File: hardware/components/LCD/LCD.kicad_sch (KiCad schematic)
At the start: 8 parts, among them SW1 slide, SW3 push

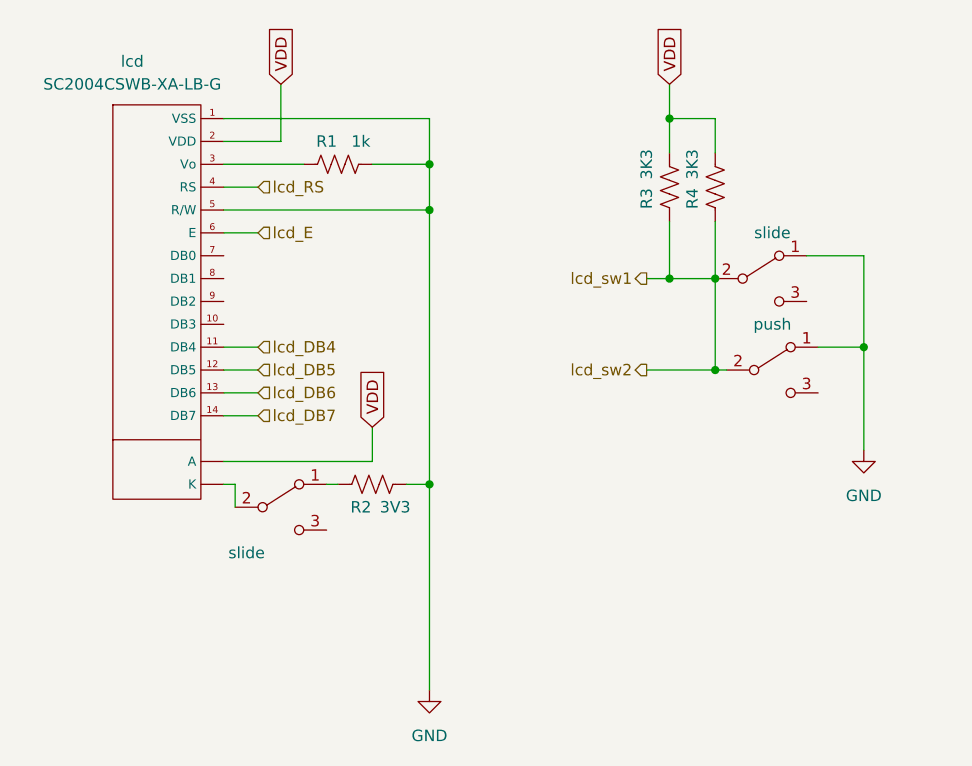
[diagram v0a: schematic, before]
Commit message: RP2040・LiPo・LoRa・ModuleIF・LCDのLCSC割り当て完了しました．基板設計中に確認していただきたいです． 何点か変更があります．LiPoPowerSimpleの充放電ICのProg周辺の抵抗値がLiPoPowerと異なっていたので合わせてしまっています． 今，ModuleIFのロードセルが指定されていたものではJLCPCBに在庫がなく，同じシリーズの在庫が多少残っているものを登録してます．そのためフットプリントと整合してません．別の物使うか判断をお願いします．
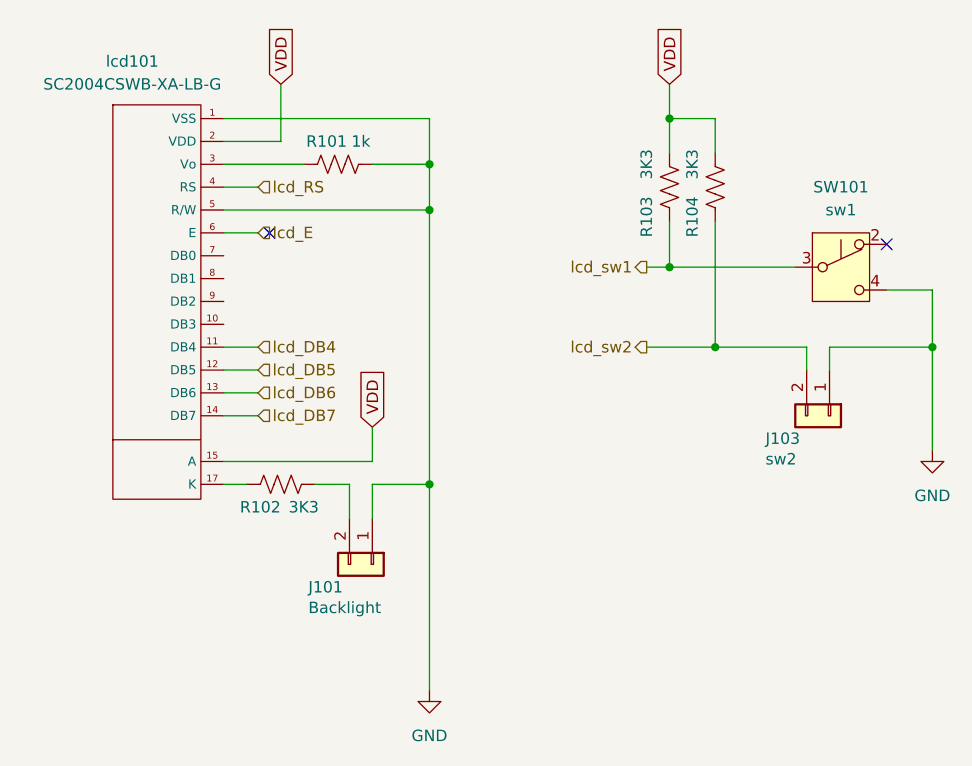
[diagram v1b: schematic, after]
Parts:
- removed SW1 (x2): slide, symbol Switch:SW_DPDT_x2
- removed SW3: push, symbol Switch:SW_DPDT_x2
- added J101: Backlight, Connector_JST:JST_PH_S2B-PH-K_1x02_P2.00mm_Horizontal, symbol Connector_Generic:Conn_01x02
- added J103: sw2, Connector_JST:JST_PH_S2B-PH-K_1x02_P2.00mm_Horizontal, symbol Connector_Generic:Conn_01x02
- added SW101: sw1, TerminalBlock_TE-Connectivity:TerminalBlock_TE_282834-5_1x05_P2.54mm_Horizontal, symbol Switch:SW_Push_SPDT
- R101: renamed from R1; footprint (none) -> Capacitor_SMD:C_0402_1005Metric; LCSC (none) -> C11702
- R102: renamed from R2; value 3V3 -> 3K3; footprint (none) -> Capacitor_SMD:C_0402_1005Metric; LCSC (none) -> C25890
- R103: renamed from R3; footprint (none) -> Capacitor_SMD:C_0402_1005Metric; LCSC (none) -> C25890
- R104: renamed from R4; footprint (none) -> Capacitor_SMD:C_0402_1005Metric; LCSC (none) -> C25890
- lcd101: renamed from lcd; footprint (none) -> WOBCLibrary:SC2004CSWB
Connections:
- net GND: now also J101.1 (Pin_1), J103.1 (Pin_1), SW101.4 (C); no longer R102.1
- net VDD: now also lcd101.15 (A); no longer lcd101. (K)
- net lcd_sw1: now also SW101.3 (B); no longer R104.2
- net at R102.2: now also lcd101.17 (K)
- new net: J101.2 (Pin_2), R102.1
- new net lcd_sw2: J103.2 (Pin_2), R104.2
- no-connect marks 0 -> 2
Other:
- moved on the sheet: R102

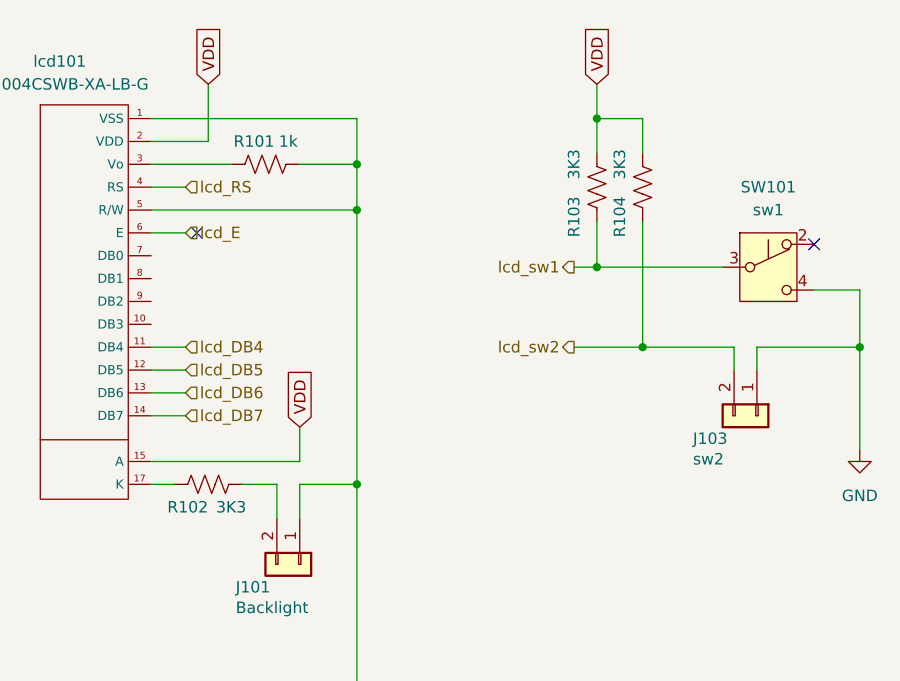
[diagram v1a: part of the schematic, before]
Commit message: ESDダイオードの変更などです。GSはまだ作りかけなので参考にしないでください
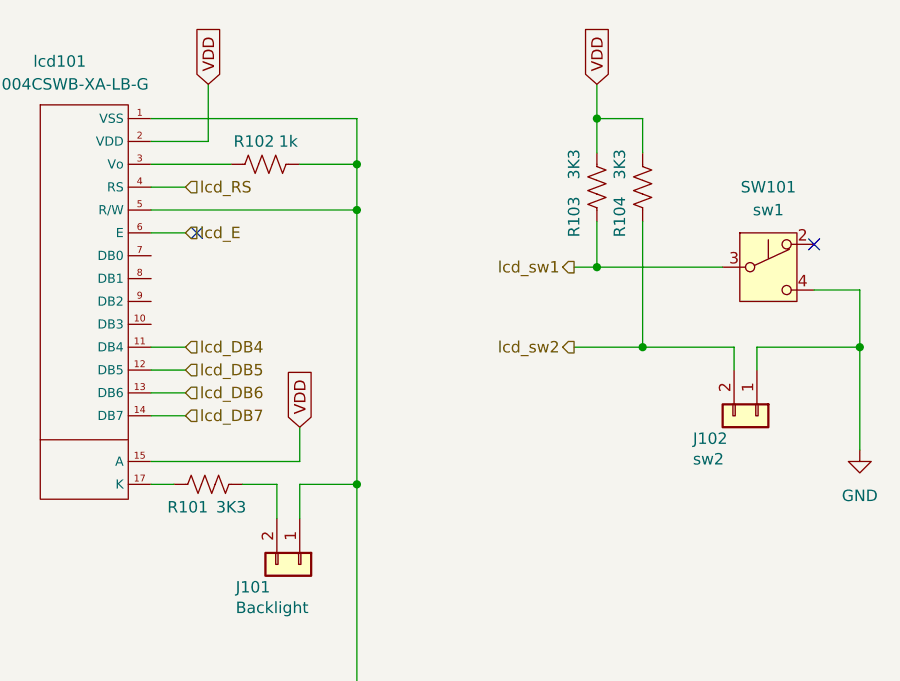
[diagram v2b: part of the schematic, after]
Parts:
- renumbered J103 to J102, R102 to R101, R101 to R102
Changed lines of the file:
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@@
 		)
 		(instances
+			(project "GS"
+				(path "/920f9ee9-d8de-4f24-ad72-1c45434a67fe/07f50231-5074-42a3-a78d-d30775b2a11d"
+					(reference "#PWR0101")
+					(unit 1)
+				)
+			)
 			(project "LCD"
 				(path "/d339b9d8-51a7-460e-bb19-8d8c25d3e2aa"
@@
 		(on_board yes)
 		(dnp no)
-		(property "Reference" "J103"
+		(property "Reference" "J102"
 			(at 192.278 123.19 90)
 			(effects
@@
 		)
 		(instances
+			(project "GS"
+				(path "/920f9ee9-d8de-4f24-ad72-1c45434a67fe/07f50231-5074-42a3-a78d-d30775b2a11d"
+					(reference "J102")
+					(unit 1)
+				)
+			)
 			(project "LCD"
 				(path "/d339b9d8-51a7-460e-bb19-8d8c25d3e2aa"
@@
 		)
 		(instances
+			(project "GS"
+				(path "/920f9ee9-d8de-4f24-ad72-1c45434a67fe/07f50231-5074-42a3-a78d-d30775b2a11d"
+					(reference "lcd101")
+					(unit 1)
+				)
+			)
 			(project "LCD"
 				(path "/d339b9d8-51a7-460e-bb19-8d8c25d3e2aa"
@@
 		)
 		(instances
+			(project "GS"
+				(path "/920f9ee9-d8de-4f24-ad72-1c45434a67fe/07f50231-5074-42a3-a78d-d30775b2a11d"
+					(reference "J101")
+					(unit 1)
+				)
+			)
 			(project "LCD"
 				(path "/d339b9d8-51a7-460e-bb19-8d8c25d3e2aa"
@@
 		(on_board yes)
 		(dnp no)
-		(property "Reference" "R102"
+		(property "Reference" "R101"
 			(at 136.144 130.81 90)
 			(effects
@@
 		)
 		(instances
+			(project "GS"
+				(path "/920f9ee9-d8de-4f24-ad72-1c45434a67fe/07f50231-5074-42a3-a78d-d30775b2a11d"
+					(reference "R101")
+					(unit 1)
+				)
+			)
 			(project "LCD"
 				(path "/d339b9d8-51a7-460e-bb19-8d8c25d3e2aa"
@@
 		)
 		(instances
+			(project "GS"
+				(path "/920f9ee9-d8de-4f24-ad72-1c45434a67fe/07f50231-5074-42a3-a78d-d30775b2a11d"
+					(reference "#PWR0102")
+					(unit 1)
+				)
+			)
 			(project "LCD"
 				(path "/d339b9d8-51a7-460e-bb19-8d8c25d3e2aa"
@@
 		)
 		(instances
+			(project "GS"
+				(path "/920f9ee9-d8de-4f24-ad72-1c45434a67fe/07f50231-5074-42a3-a78d-d30775b2a11d"
+					(reference "R104")
+					(unit 1)
+				)
+			)
 			(project "LCD"
 				(path "/d339b9d8-51a7-460e-bb19-8d8c25d3e2aa"
@@
 		(on_board yes)
 		(dnp no)
-		(property "Reference" "R101"
+		(property "Reference" "R102"
 			(at 143.51 90.17 90)
 			(effects
@@
 		)
 		(instances
+			(project "GS"
+				(path "/920f9ee9-d8de-4f24-ad72-1c45434a67fe/07f50231-5074-42a3-a78d-d30775b2a11d"
+					(reference "R102")
+					(unit 1)
+				)
+			)
 			(project "LCD"
 				(path "/d339b9d8-51a7-460e-bb19-8d8c25d3e2aa"
@@
 		)
 		(instances
+			(project "GS"
+				(path "/920f9ee9-d8de-4f24-ad72-1c45434a67fe/07f50231-5074-42a3-a78d-d30775b2a11d"
+					(reference "SW101")
+					(unit 1)
+				)
+			)
 			(project "LCD"
 				(path "/d339b9d8-51a7-460e-bb19-8d8c25d3e2aa"
@@
 		)
 		(instances
-			(project "LCD"
-				(path "/d339b9d8-51a7-460e-bb19-8d8c25d3e2aa"
+			(project "GS"
+				(path "/920f9ee9-d8de-4f24-ad72-1c45434a67fe/07f50231-5074-42a3-a78d-d30775b2a11d"
 					(reference "R103")
 					(unit 1)
 				)
 			)
-		)
-	)
-	(sheet_instances
-		(path "/"
-			(page "1")
-		)
-	)
+			(project "LCD"
+				(path "/d339b9d8-51a7-460e-bb19-8d8c25d3e2aa"
+					(reference "R103")
+					(unit 1)
+				)
+			)
+		)
+	)

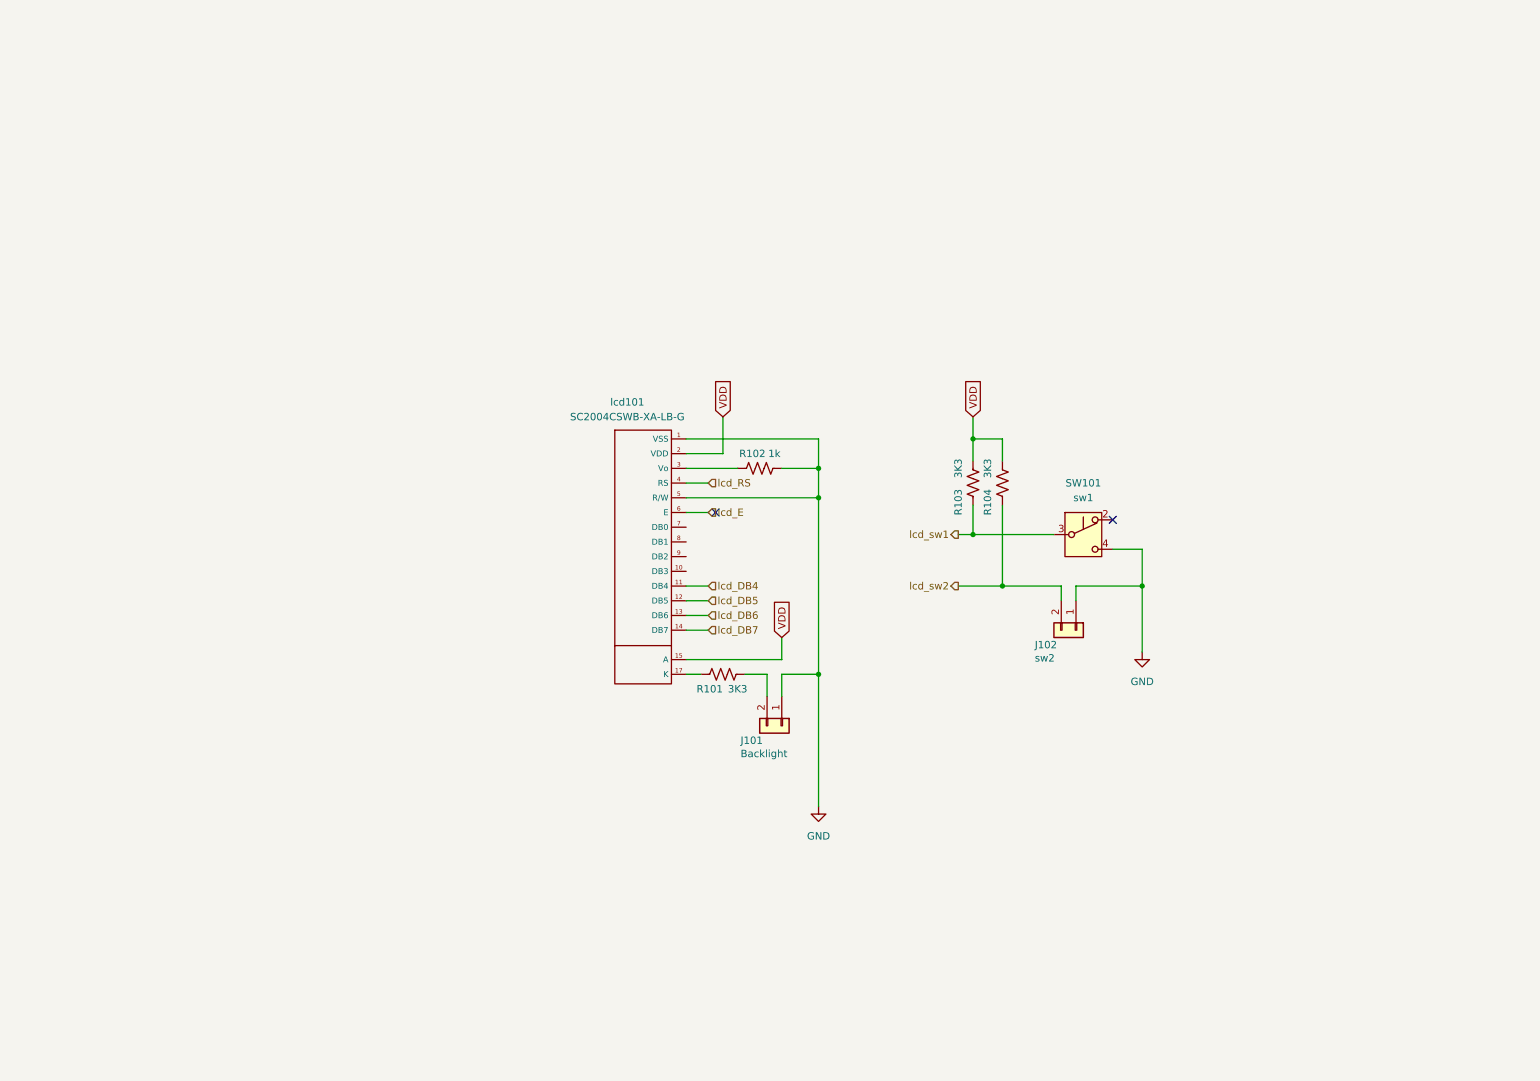
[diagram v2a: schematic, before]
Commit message: LCD基板の大幅変更とそれに伴うフットプリント・シンボルライブラリの追加
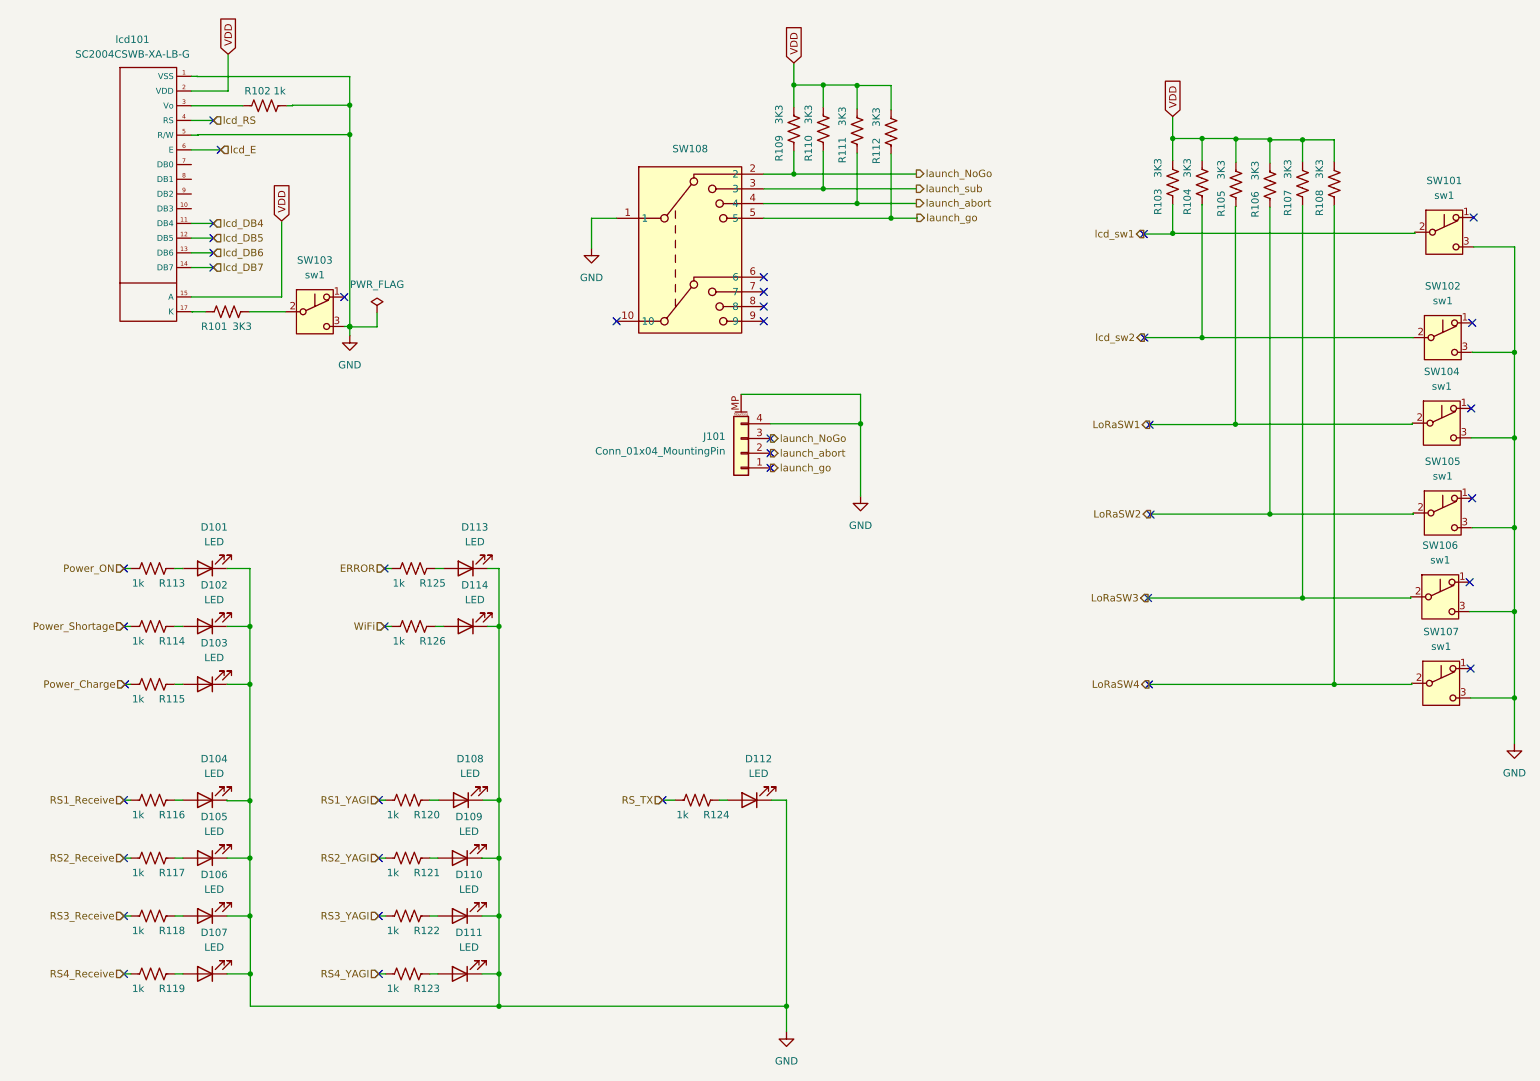
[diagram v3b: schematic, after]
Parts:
- removed J101: Backlight, Connector_JST:JST_PH_S2B-PH-K_1x02_P2.00mm_Horizontal, symbol Connector_Generic:Conn_01x02
- removed J102: sw2, Connector_JST:JST_PH_S2B-PH-K_1x02_P2.00mm_Horizontal, symbol Connector_Generic:Conn_01x02
- added D101, D102, D103, D104, D105, D106, D107, D108, D109, D110, D111, D112, D113, D114: LED, LED_THT:LED_D3.0mm_FlatTop, symbol Device:LED
- added J101: Conn_01x04_MountingPin, WOBCLibrary:Grove_4P_L_SMD, symbol Connector_Generic_MountingPin:Conn_01x04_MountingPin
- added R105, R106, R107, R108, R109, R110, R111, R112: 3K3, Capacitor_SMD:C_0402_1005Metric, symbol Device:R_US
- added R113, R114, R115, R116, R117, R118, R119, R120, R121, R122, R123, R124, R125, R126: 1k, Capacitor_SMD:C_0402_1005Metric, symbol Device:R_US
- added SW102, SW103, SW104, SW105, SW106, SW107: sw1, WOBCLibrary:ToggleSwitch, symbol Switch:SW_Push_SPDT
- added SW108: ~, WOBCLibrary:RotarySwitch_2x04, symbol WOBCLibrary:RotarySwitch2x04
- SW101: footprint TerminalBlock_TE-Connectivity:TerminalBlock_TE_282834-5_1x05_P2.54mm_Horizontal -> WOBCLibrary:ToggleSwitch
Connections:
- net GND: now also SW101.3 (C), D101.1 (K), D102.1 (K), D103.1 (K), D104.1 (K), D105.1 (K), D106.1 (K), D107.1 (K), D108.1 (K), D109.1 (K), D110.1 (K), D111.1 (K), D112.1 (K), D113.1 (K), D114.1 (K), J101.4 (Pin_4), J101.MP (MountPin), SW102.3 (C), SW103.3 (C), SW104.3 (C), SW105.3 (C), SW106.3 (C), SW107.3 (C), SW108.1; no longer SW101.4 (C)
- net VDD: now also R105.1, R106.1, R107.1, R108.1, R109.1, R110.1, R111.1, R112.1
- net lcd_sw1: now also SW101.2 (B); no longer SW101.3 (B)
- net lcd_sw2: now also SW102.2 (B)
- net at R101.1: now also SW103.2 (B)
- new net: D112.2 (A), R124.2
- new net: D111.2 (A), R123.2
- new net: D105.2 (A), R117.2
- new net: D110.2 (A), R122.2
- new net: D103.2 (A), R115.2
- new net: D104.2 (A), R116.2
- new net: D101.2 (A), R113.2
- new net: D107.2 (A), R119.2
- new net: D114.2 (A), R126.2
- new net: D113.2 (A), R125.2
- new net: D102.2 (A), R114.2
- new net: D109.2 (A), R121.2
- new net: D108.2 (A), R120.2
- new net: D106.2 (A), R118.2
- new net ERROR: R125.1
- new net LoRaSW1: R105.2, SW104.2 (B)
- new net LoRaSW2: R106.2, SW105.2 (B)
- new net LoRaSW3: R107.2, SW106.2 (B)
- new net LoRaSW4: R108.2, SW107.2 (B)
- new net Power_Charge: R115.1
- new net Power_ON: R113.1
- new net Power_Shortage: R114.1
- new net RS1_Receive: R116.1
- new net RS1_YAGI: R120.1
- new net RS2_Receive: R117.1
- new net RS2_YAGI: R121.1
- new net RS3_Receive: R118.1
- new net RS3_YAGI: R122.1
- new net RS4_Receive: R119.1
- new net RS4_YAGI: R123.1
- new net RS_TX: R124.1
- new net WiFi: R126.1
- new net launch_NoGo: J101.3 (Pin_3), R109.2, SW108.2
- new net launch_abort: J101.2 (Pin_2), R111.2, SW108.4
- new net launch_go: J101.1 (Pin_1), R112.2, SW108.5
- new net launch_sub: R110.2, SW108.3
- no-connect marks 2 -> 41
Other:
- moved on the sheet: R101, R102, R103, R104, SW101, lcd101
